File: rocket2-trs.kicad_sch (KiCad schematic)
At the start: 50 parts, among them J2 SMA, J3 ARM Cortex Debug, J4 Conn_01x12_MountingPin, J5 Conn_01x12_MountingPin, U4 AZ1117-3.3, U5 LoRA-E5, Y1 16MHz

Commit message: added test points, removed connectors
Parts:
- removed J4, J5: Conn_01x12_MountingPin, symbol Connector_Generic_MountingPin:Conn_01x12_MountingPin
- added TP21: UART1 TX, TestPoint:TestPoint_Pad_D1.0mm, symbol Connector:TestPoint
- added TP22: UART1 RX, TestPoint:TestPoint_Pad_D1.0mm, symbol Connector:TestPoint
- added TP23: LORA_RST, TestPoint:TestPoint_Pad_D1.0mm, symbol Connector:TestPoint
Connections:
- net ETH_RX: now also U5.21 (RX1_(PC0)); no longer U5.20 (RX1_(PC0))
- net ETH_TX: now also U5.22 (TX1_(PC1)); no longer U5.21 (TX1_(PC1))
- net ETH_nRST: now also U5.20 (D0_(PA0)); no longer U5.19 (D0_(PA0))
- net GND: now also U5.13 (GND); no longer U5.12 (GND)
- net LORA_RST: now also TP23.1
- net UART1 RX: now also U5.18 (RX_(PB7)), TP22.1; no longer U5.17 (RX_(PB7))
- net UART1 TX: now also U5.19 (TX_(PB6)), TP21.1; no longer U5.18 (TX_(PB6))
- no-connect marks 47 -> 33

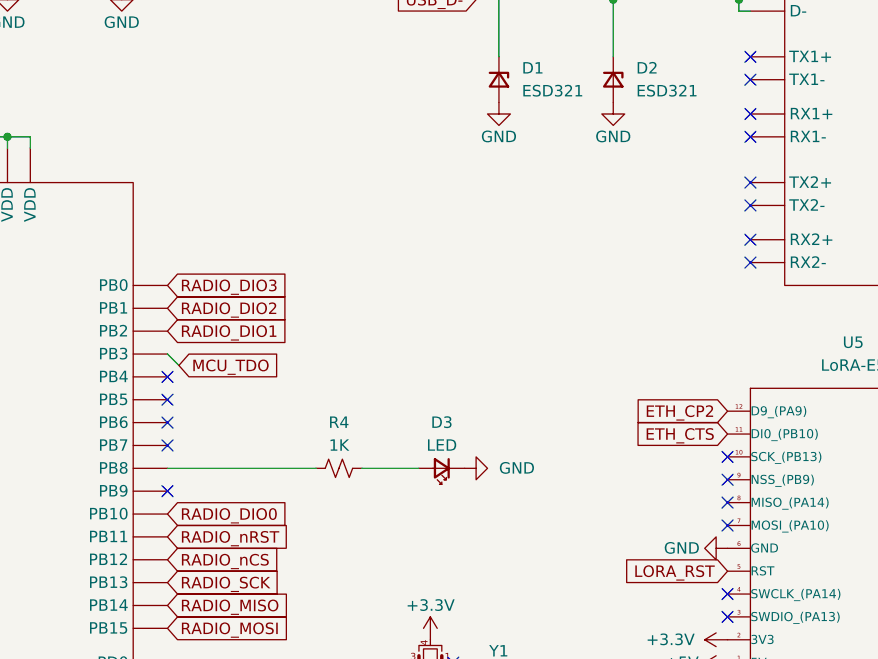
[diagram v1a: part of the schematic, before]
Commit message: adding nmos
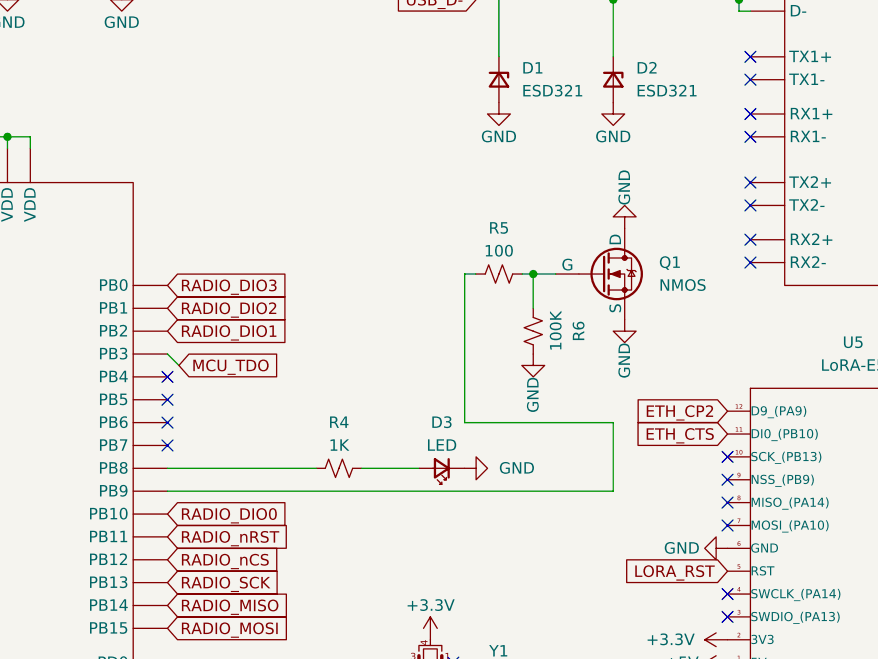
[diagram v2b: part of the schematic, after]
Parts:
- added Q1: NMOS, symbol Simulation_SPICE:NMOS
- added R5: 100, Resistor_SMD:R_0603_1608Metric, symbol Device:R_Small_US
- added R6: 100K, Resistor_SMD:R_0603_1608Metric, symbol Device:R_Small_US
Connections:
- net GND: now also Q1.1 (D), Q1.3 (S), R6.2
- net at U1.46 (PB9): now also R5.1
- new net: Q1.2 (G), R5.2, R6.1
- no-connect marks 33 -> 32

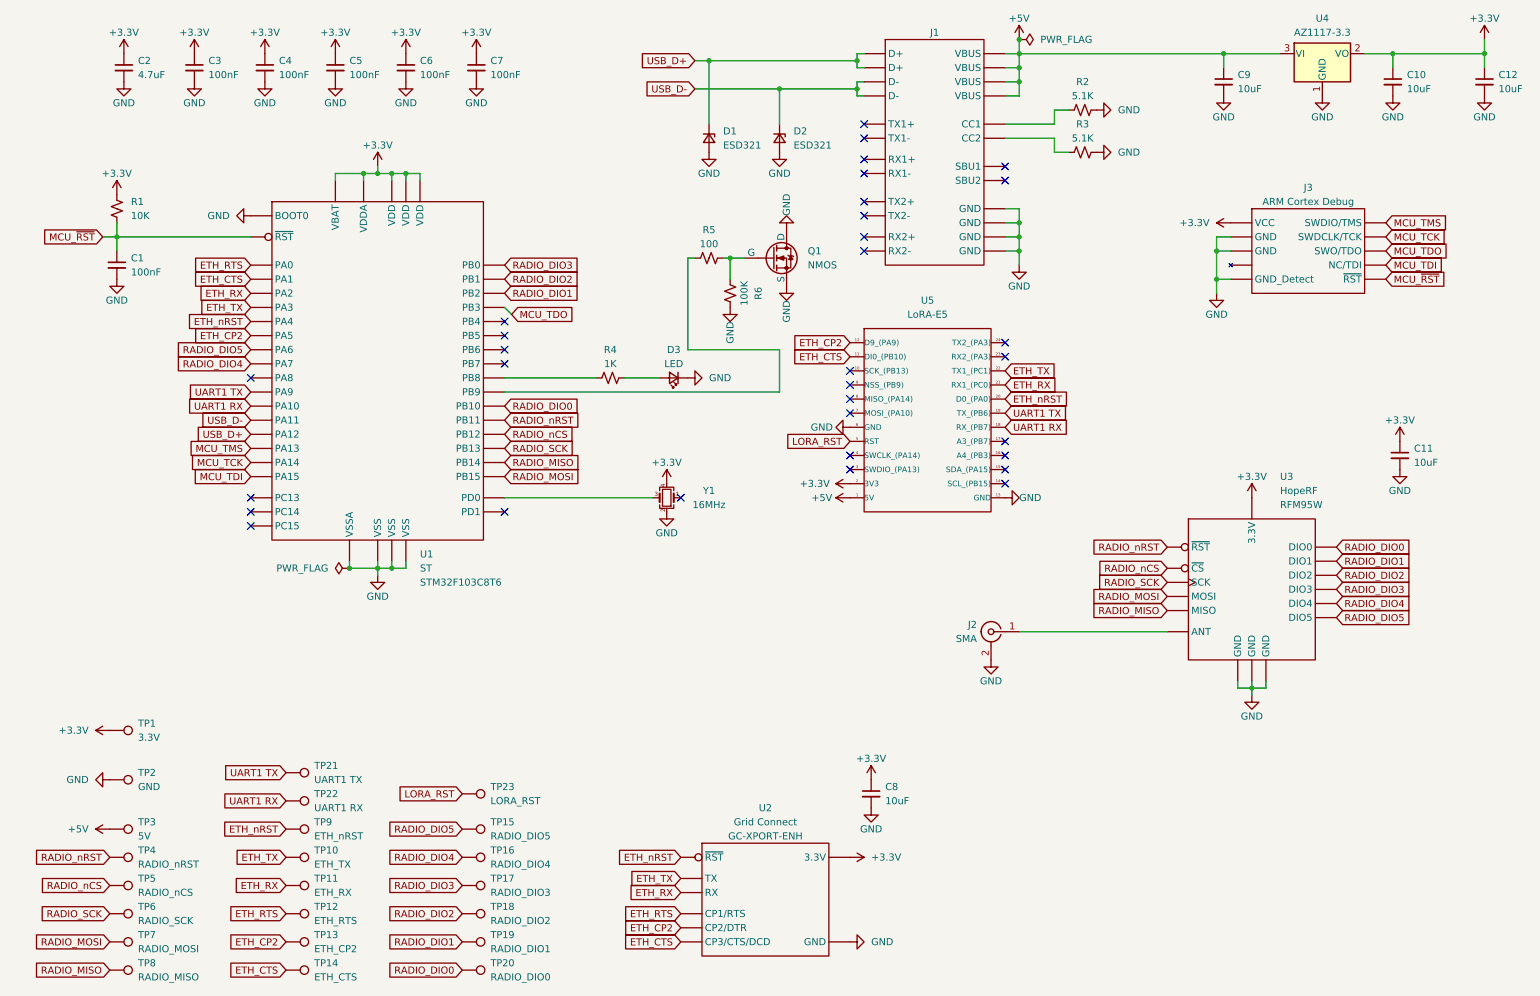
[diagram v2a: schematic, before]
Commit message: added nmos and fixed rx tx
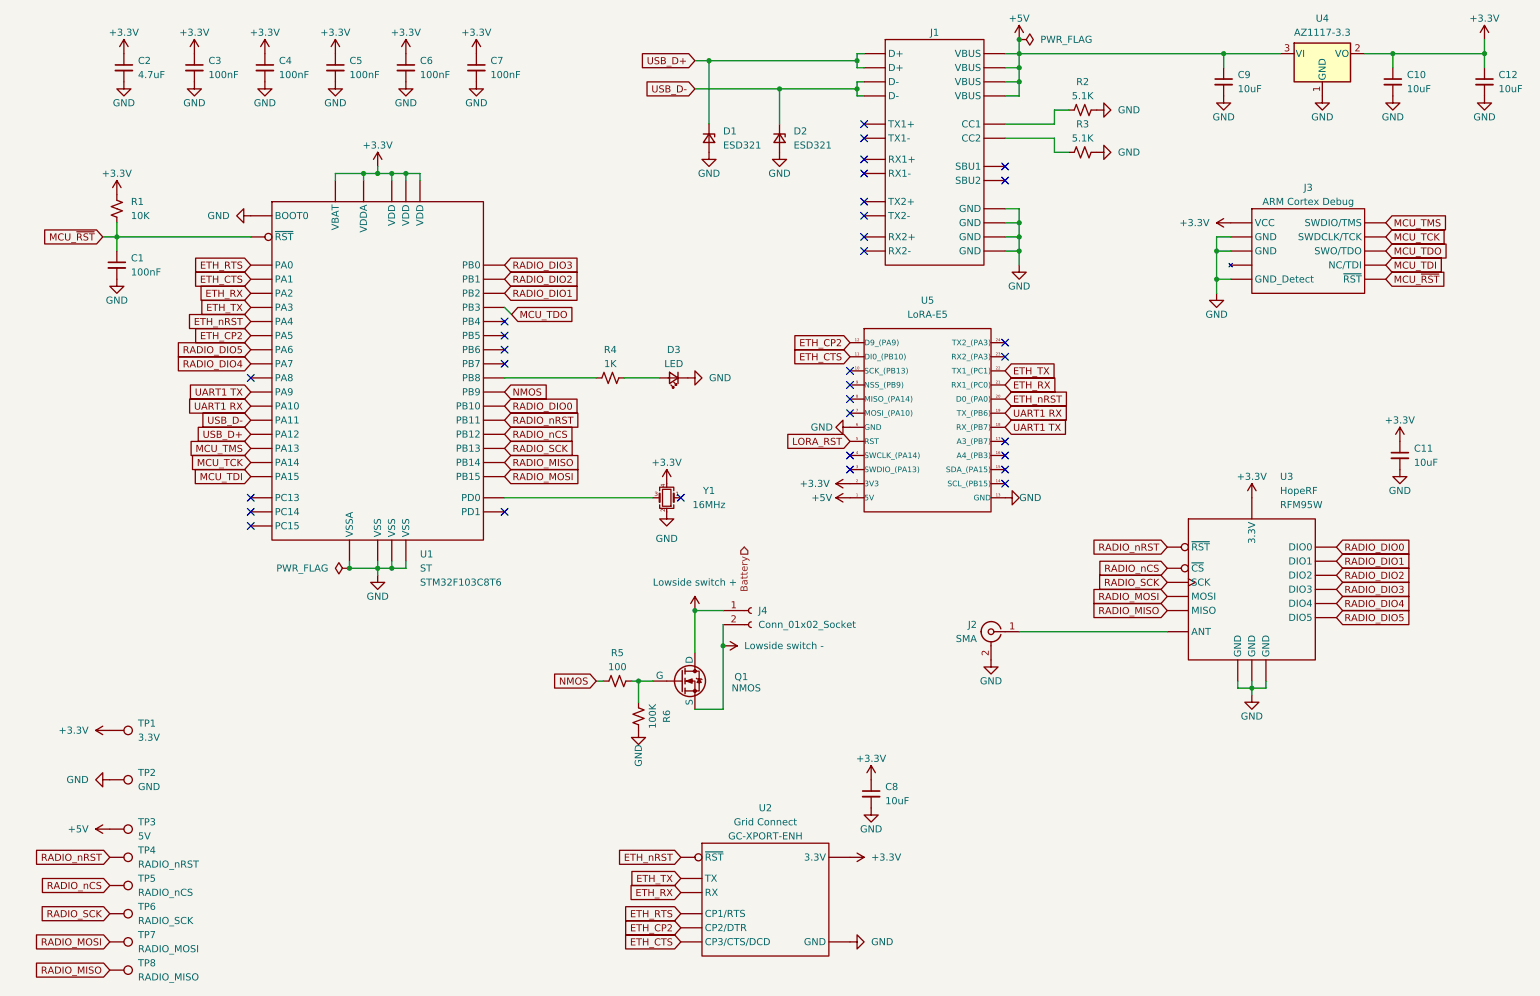
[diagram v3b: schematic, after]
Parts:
- removed TP10: ETH_TX, TestPoint:TestPoint_Pad_D1.0mm, symbol Connector:TestPoint
- removed TP11: ETH_RX, TestPoint:TestPoint_Pad_D1.0mm, symbol Connector:TestPoint
- removed TP12: ETH_RTS, TestPoint:TestPoint_Pad_D1.0mm, symbol Connector:TestPoint
- removed TP13: ETH_CP2, TestPoint:TestPoint_Pad_D1.0mm, symbol Connector:TestPoint
- removed TP14: ETH_CTS, TestPoint:TestPoint_Pad_D1.0mm, symbol Connector:TestPoint
- removed TP15: RADIO_DIO5, TestPoint:TestPoint_Pad_D1.0mm, symbol Connector:TestPoint
- removed TP16: RADIO_DIO4, TestPoint:TestPoint_Pad_D1.0mm, symbol Connector:TestPoint
- removed TP17: RADIO_DIO3, TestPoint:TestPoint_Pad_D1.0mm, symbol Connector:TestPoint
- removed TP18: RADIO_DIO2, TestPoint:TestPoint_Pad_D1.0mm, symbol Connector:TestPoint
- removed TP19: RADIO_DIO1, TestPoint:TestPoint_Pad_D1.0mm, symbol Connector:TestPoint
- removed TP20: RADIO_DIO0, TestPoint:TestPoint_Pad_D1.0mm, symbol Connector:TestPoint
- removed TP21: UART1 TX, TestPoint:TestPoint_Pad_D1.0mm, symbol Connector:TestPoint
- removed TP22: UART1 RX, TestPoint:TestPoint_Pad_D1.0mm, symbol Connector:TestPoint
- removed TP23: LORA_RST, TestPoint:TestPoint_Pad_D1.0mm, symbol Connector:TestPoint
- removed TP9: ETH_nRST, TestPoint:TestPoint_Pad_D1.0mm, symbol Connector:TestPoint
- added J4: Conn_01x02_Socket, Connector_PinSocket_1.27mm:PinSocket_1x02_P1.27mm_Vertical, symbol Connector:Conn_01x02_Socket
- Q1: footprint (none) -> Package_TO_SOT_SMD:SOT-23
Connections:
- net GND: no longer Q1.1 (D), Q1.3 (S)
- net UART1 RX: now also U5.19 (TX_(PB6)); no longer U5.18 (RX_(PB7))
- net UART1 TX: now also U5.18 (RX_(PB7)); no longer U5.19 (TX_(PB6))
- net NMOS: now reaches R5.1, U1.46 (PB9)
- net at R5.2, R6.1: now also Q1.1 (G); no longer Q1.2 (G)
- new net Lowside switch +: J4.1 (Pin_1), Q1.3 (D)
- new net Lowside switch -: J4.2 (Pin_2), Q1.2 (S)
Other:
- moved on the sheet: Q1, R5, R6

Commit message: Fixed board size and removed eth from lora
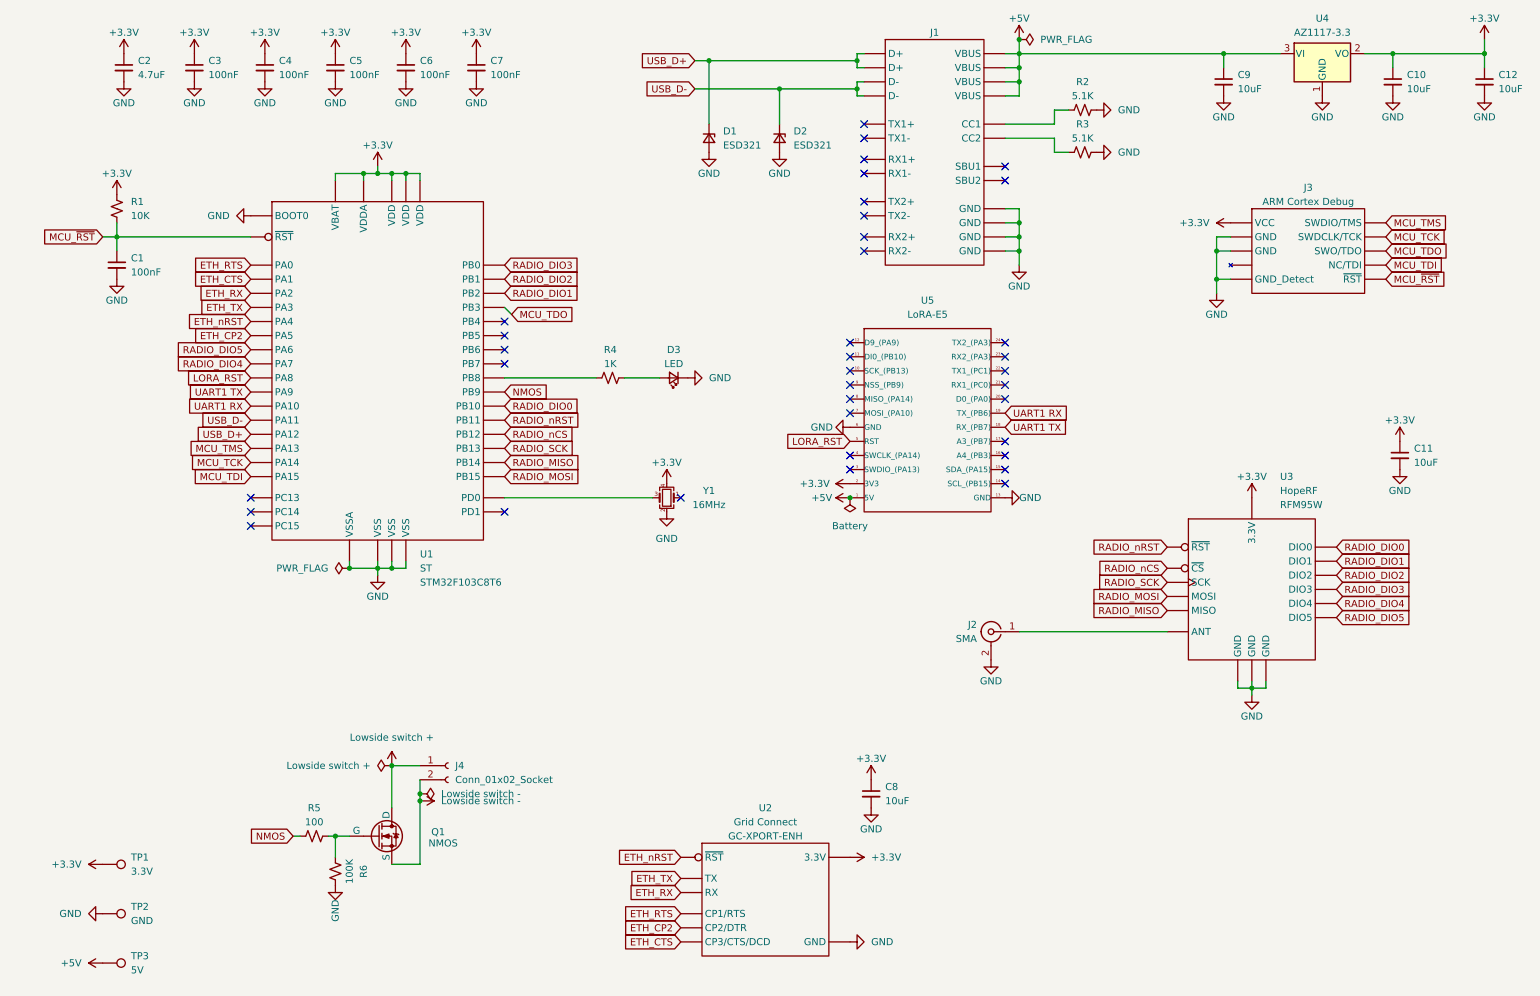
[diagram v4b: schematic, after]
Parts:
- removed TP4: RADIO_nRST, TestPoint:TestPoint_Pad_D1.0mm, symbol Connector:TestPoint
- removed TP5: RADIO_nCS, TestPoint:TestPoint_Pad_D1.0mm, symbol Connector:TestPoint
- removed TP6: RADIO_SCK, TestPoint:TestPoint_Pad_D1.0mm, symbol Connector:TestPoint
- removed TP7: RADIO_MOSI, TestPoint:TestPoint_Pad_D1.0mm, symbol Connector:TestPoint
- removed TP8: RADIO_MISO, TestPoint:TestPoint_Pad_D1.0mm, symbol Connector:TestPoint
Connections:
- net ETH_CP2: no longer U5.12 (D9_(PA9))
- net ETH_CTS: no longer U5.11 (DI0_(PB10))
- net ETH_RX: no longer U5.21 (RX1_(PC0))
- net ETH_TX: no longer U5.22 (TX1_(PC1))
- net ETH_nRST: no longer U5.20 (D0_(PA0))
- net LORA_RST: now also U1.29 (PA8)
- no-connect marks 32 -> 36
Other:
- moved on the sheet: J4, Q1, R5, R6, TP1, TP2, TP3
